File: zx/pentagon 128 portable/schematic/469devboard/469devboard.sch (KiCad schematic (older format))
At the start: 75 parts, among them IC1 1072, J1 Conn_02x17_Odd_Even, J11 DSI, J2 Conn_ARM_JTAG_SWD_20, J3 10033526-N3212LF, J4 Conn_01x03_Male, J5 Conn_01x35_Male, J6 Conn_01x36_Male, J7 Conn_01x23_Male, J8 Conn_01x30_Male, J9 104031-0811, SW1 SW_Push, U1 STM32F469IITx, U2 LD1117S33TR_SOT223, Y1 Q13FC1350000400, Y2 ABM3B-8.000MHZ-10-1-U-T

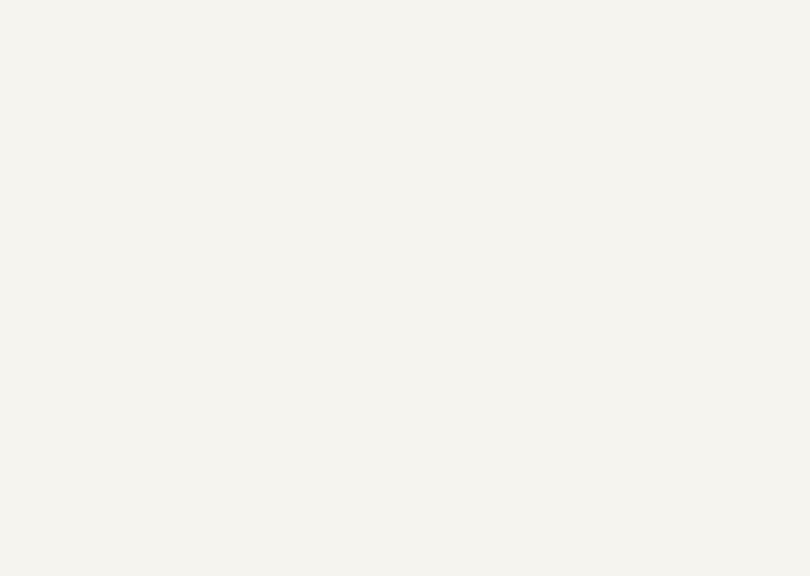
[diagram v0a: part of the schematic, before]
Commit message: added memory devboard, moved devboard to schematic
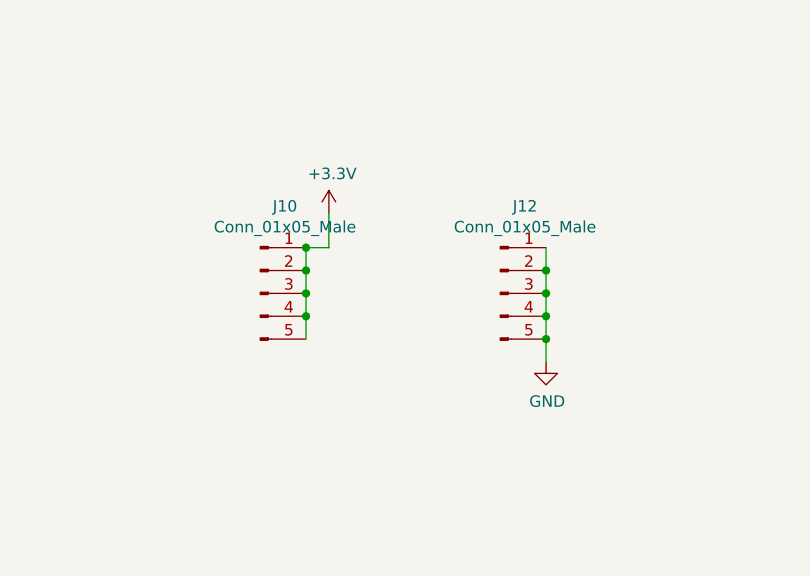
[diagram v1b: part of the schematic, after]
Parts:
- added J10, J12: Conn_01x05_Male, Connector_PinHeader_2.54mm:PinHeader_1x05_P2.54mm_Vertical, symbol Connector:Conn_01x05_Male
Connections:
- wire segments 388 -> 399
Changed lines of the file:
@@
 	1    0    0    -1
 $EndComp
+$Comp
+L Connector:Conn_01x05_Male J10
+U 1 1 5F70DAB7
+P -3050 2000
+F 0 "J10" H -2942 2381 50  0000 C CNN
+F 1 "Conn_01x05_Male" H -2942 2290 50  0000 C CNN
+F 2 "Connector_PinHeader_2.54mm:PinHeader_1x05_P2.54mm_Vertical" H -3050 2000 50  0001 C CNN
+F 3 "~" H -3050 2000 50  0001 C CNN
+	1    -3050 2000
+	1    0    0    -1
+$EndComp
+$Comp
+L Connector:Conn_01x05_Male J12
+U 1 1 5F70E84C
+P -2000 2000
+F 0 "J12" H -1892 2381 50  0000 C CNN
+F 1 "Conn_01x05_Male" H -1892 2290 50  0000 C CNN
+F 2 "Connector_PinHeader_2.54mm:PinHeader_1x05_P2.54mm_Vertical" H -2000 2000 50  0001 C CNN
+F 3 "~" H -2000 2000 50  0001 C CNN
+	1    -2000 2000
+	1    0    0    -1
+$EndComp
+$Comp
+L power:GND #PWR0127
+U 1 1 5F70F2D5
+P -1800 2300
+F 0 "#PWR0127" H -1800 2050 50  0001 C CNN
+F 1 "GND" H -1795 2127 50  0000 C CNN
+F 2 "" H -1800 2300 50  0001 C CNN
+F 3 "" H -1800 2300 50  0001 C CNN
+	1    -1800 2300
+	1    0    0    -1
+$EndComp
+$Comp
+L power:+3.3V #PWR0129
+U 1 1 5F71015A
+P -2750 1650
+F 0 "#PWR0129" H -2750 1500 50  0001 C CNN
+F 1 "+3.3V" H -2735 1823 50  0000 C CNN
+F 2 "" H -2750 1650 50  0001 C CNN
+F 3 "" H -2750 1650 50  0001 C CNN
+	1    -2750 1650
+	1    0    0    -1
+$EndComp
+Wire Wire Line
+	-2850 1800 -2850 1900
+Wire Wire Line
+	-2850 1900 -2850 2000
+Connection ~ -2850 1900
+Wire Wire Line
+	-2850 2100 -2850 2000
+Connection ~ -2850 2000
+Wire Wire Line
+	-2850 2100 -2850 2200
+Connection ~ -2850 2100
+Wire Wire Line
+	-2850 1800 -2750 1800
+Wire Wire Line
+	-2750 1800 -2750 1650
+Connection ~ -2850 1800
+Wire Wire Line
+	-1800 1800 -1800 1900
+Wire Wire Line
+	-1800 1900 -1800 2000
+Connection ~ -1800 1900
+Wire Wire Line
+	-1800 2100 -1800 2000
+Connection ~ -1800 2000
+Wire Wire Line
+	-1800 2100 -1800 2200
+Connection ~ -1800 2100
+Wire Wire Line
+	-1800 2200 -1800 2300
+Connection ~ -1800 2200
 $EndSCHEMATC

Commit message: pentagon
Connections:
- net labels removed: +3.3
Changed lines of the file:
@@
 GND
 Text Label 6200 2850 0    50   ~ 0
-+3.3
++3.3V
 Text Label 7050 3850 0    50   ~ 0
 FMC_D0
@@
 	-1800 2200 -1800 2300
 Connection ~ -1800 2200
+Text Label 7050 2950 0    50   ~ 0
++3.3V
+Text Label 7100 2850 0    50   ~ 0
+GND
 $EndSCHEMATC
